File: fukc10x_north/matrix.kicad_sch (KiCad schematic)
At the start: 247 parts

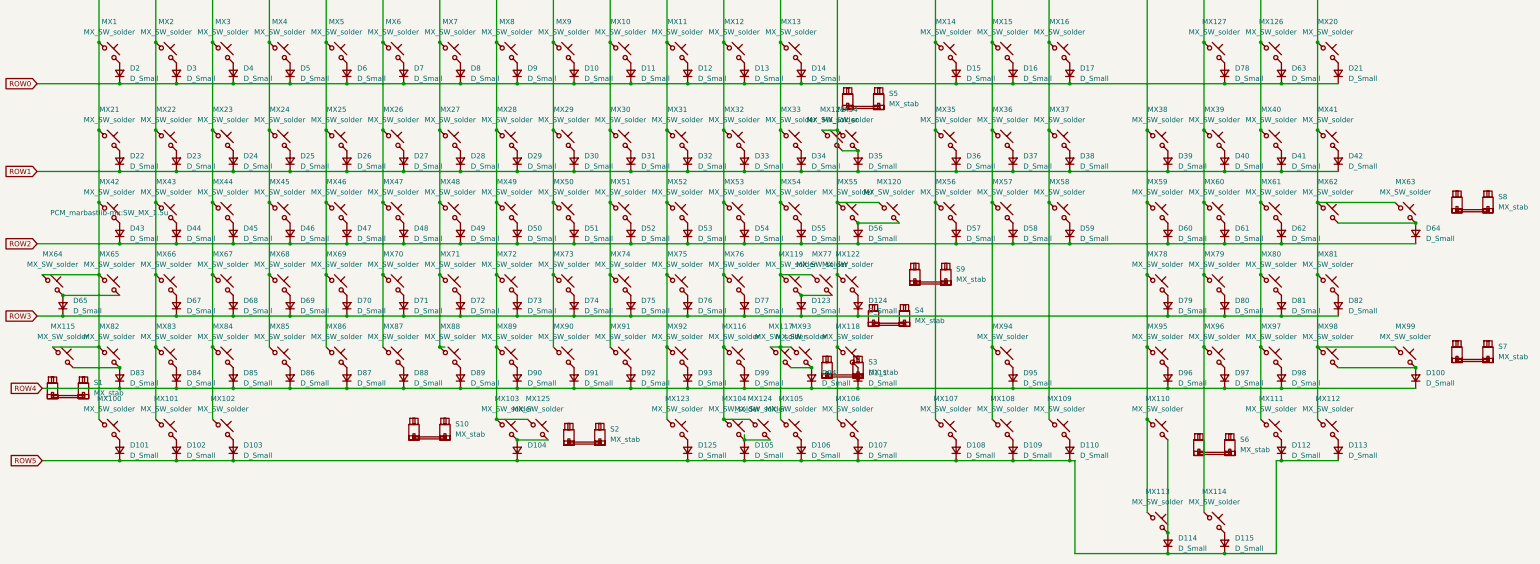
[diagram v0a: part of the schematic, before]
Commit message: updated parts for bom and stuff
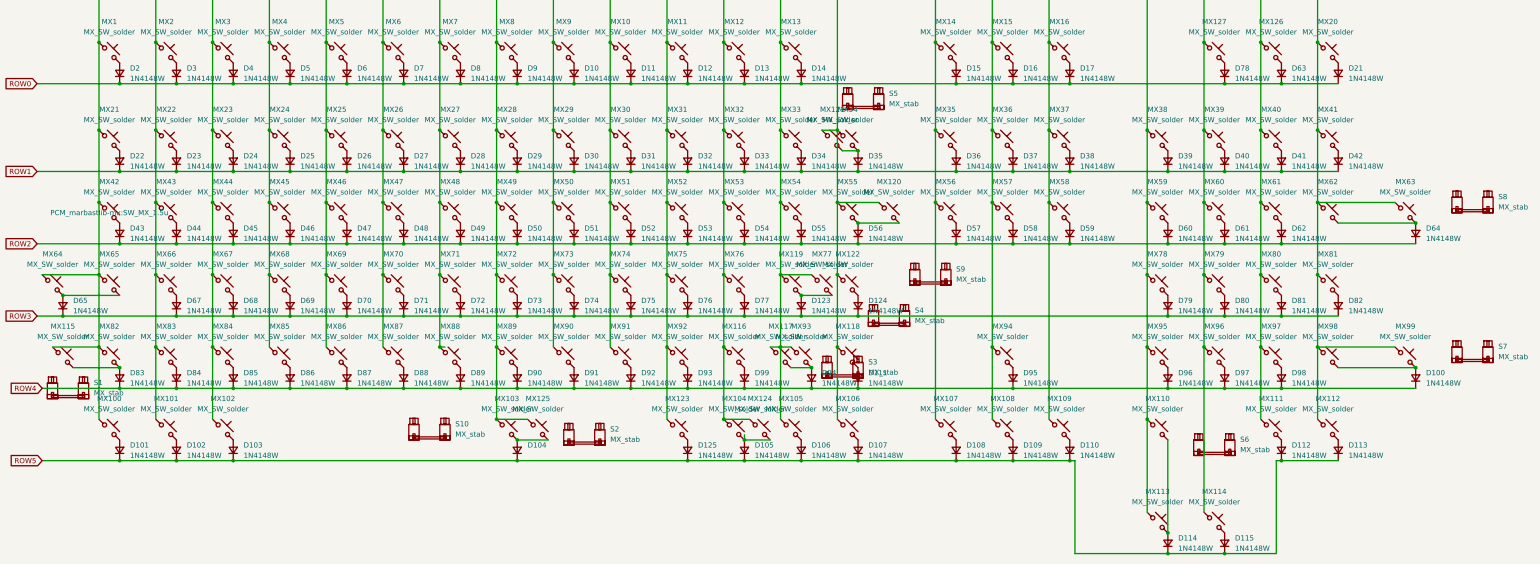
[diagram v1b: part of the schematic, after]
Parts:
- D10, D100, D101, D102, D103, D104, D105, D106, D107, D108, D109, D11, D110, D111, D112, D113, D114, D115, D12, D123, D124, D125, D13, D14, D15, D16, D17, D2, D21, D22, D23, D24, D25, D26, D27, D28, D29, D3, D30, D31, D32, D33, D34, D35, D36, D37, D38, D39, D4, D40, D41, D42, D43, D44, D45, D46, D47, D48, D49, D5, D50, D51, D52, D53, D54, D55, D56, D57, D58, D59, D6, D60, D61, D62, D63, D64, D65, D67, D68, D69, D7, D70, D71, D72, D73, D74, D75, D76, D77, D78, D79, D8, D80, D81, D82, D83, D84, D85, D86, D87, D88, D89, D9, D90, D91, D92, D93, D94, D95, D96, D97, D98, D99: value D_Small -> 1N4148W
- MX1, MX10, MX100, MX101, MX102, MX103, MX104, MX105, MX106, MX107, MX108, MX109, MX11, MX110, MX111, MX112, MX113, MX114, MX115, MX116, MX117, MX118, MX119, MX12, MX120, MX121, MX122, MX123, MX124, MX125, MX126, MX127, MX13, MX14, MX15, MX16, MX2, MX20, MX21, MX22, MX23, MX24, MX25, MX26, MX27, MX28, MX29, MX3, MX30, MX31, MX32, MX33, MX34, MX35, MX36, MX37, MX38, MX39, MX4, MX40, MX41, MX42, MX43, MX44, MX45, MX46, MX47, MX48, MX49, MX5, MX50, MX51, MX52, MX53, MX54, MX55, MX56, MX57, MX58, MX59, MX6, MX60, MX61, MX62, MX63, MX64, MX65, MX66, MX67, MX68, MX69, MX7, MX70, MX71, MX72, MX73, MX74, MX75, MX76, MX77, MX78, MX79, MX8, MX80, MX81, MX82, MX83, MX84, MX85, MX86, MX87, MX88, MX89, MX9, MX90, MX91, MX92, MX93, MX94, MX95, MX96, MX97, MX98, MX99, S1, S10, S2, S3, S4, S5, S6, S7, S8, S9: now left out of the parts list

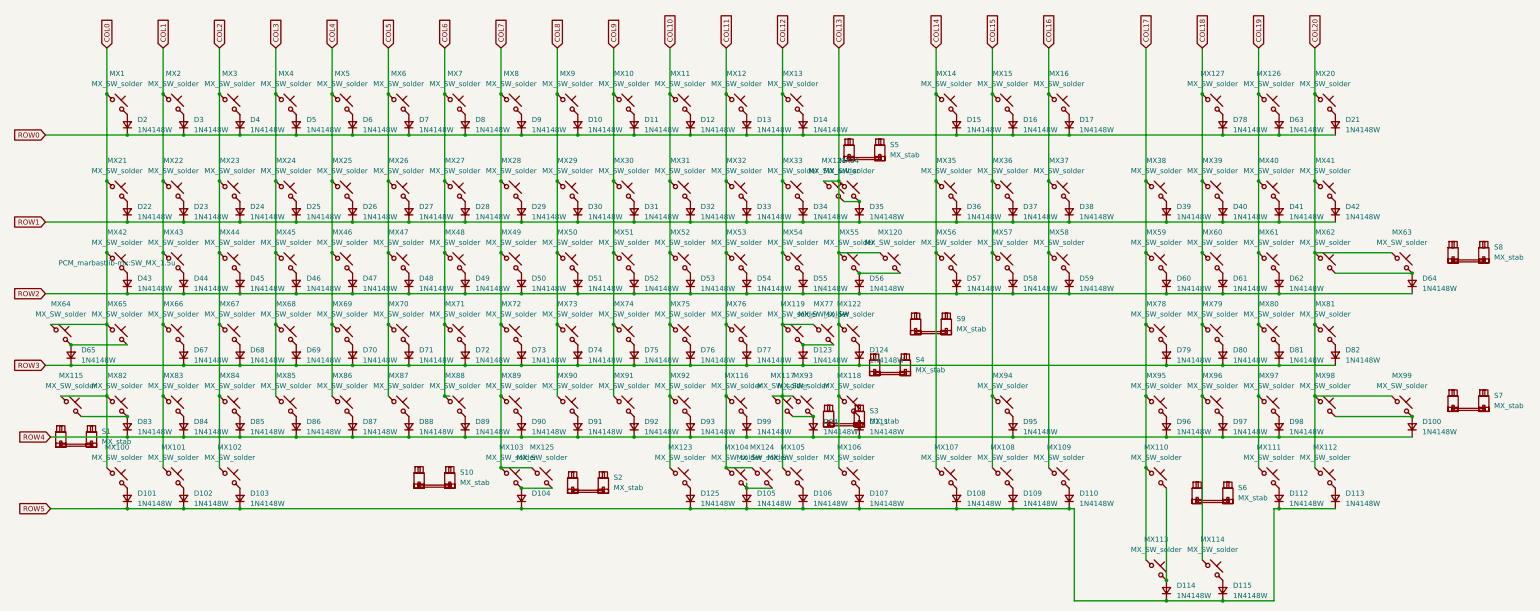
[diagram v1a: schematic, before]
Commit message: fixed some routing, changed footprints from marbastler to acheron alexandria lib (although with rotated switches(kinda cursed))
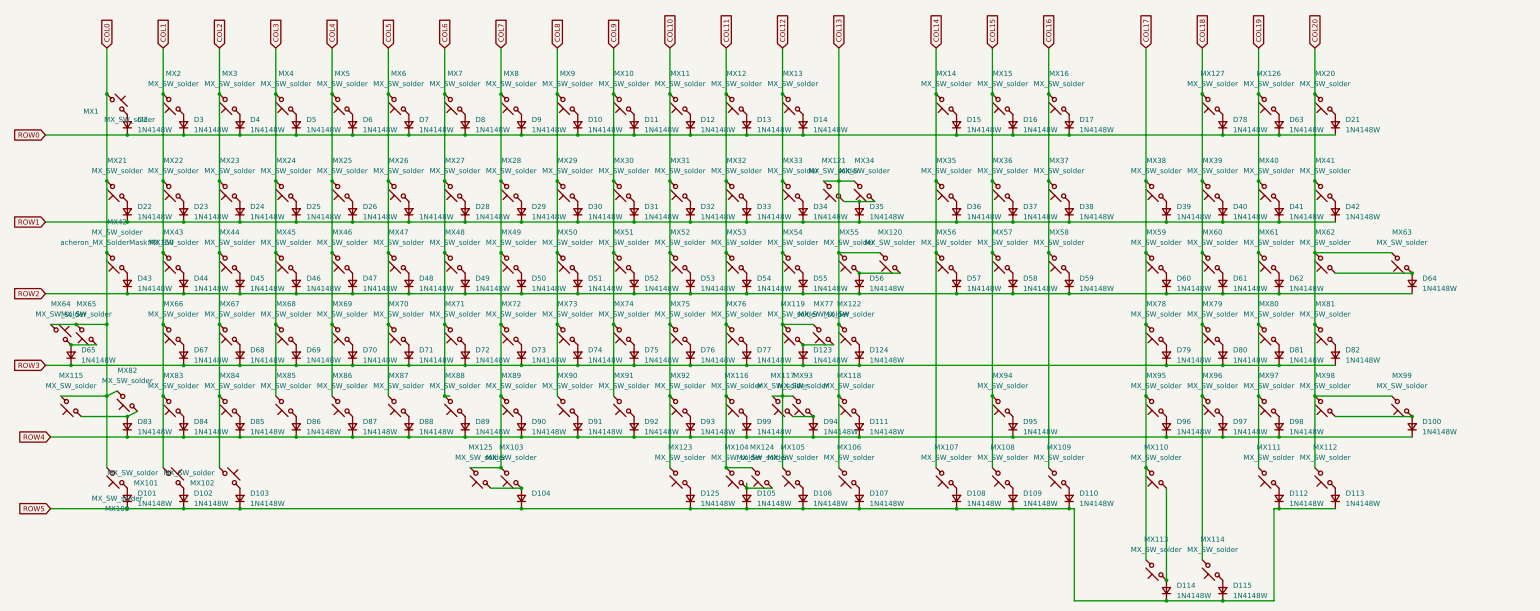
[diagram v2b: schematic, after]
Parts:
- removed S1, S4: MX_stab, PCM_marbastlib-mx:STAB_MX_2.25u, symbol PCM_marbastlib-mx:MX_stab
- removed S10: MX_stab, PCM_marbastlib-mx:STAB_MX_6u, symbol PCM_marbastlib-mx:MX_stab
- removed S2: MX_stab, PCM_marbastlib-mx:STAB_MX_7u, symbol PCM_marbastlib-mx:MX_stab
- removed S3: MX_stab, PCM_marbastlib-mx:STAB_MX_2.75u, symbol PCM_marbastlib-mx:MX_stab
- removed S5, S6, S7, S8: MX_stab, PCM_marbastlib-mx:STAB_MX_2u, symbol PCM_marbastlib-mx:MX_stab
- removed S9: MX_stab, PCM_marbastlib-mx:STAB_MX_ISO-ROT, symbol PCM_marbastlib-mx:MX_stab
- MX1, MX10, MX101, MX105, MX107, MX108, MX109, MX11, MX110, MX111, MX112, MX113, MX114, MX116, MX118, MX119, MX12, MX121, MX122, MX124, MX126, MX127, MX13, MX14, MX15, MX16, MX2, MX20, MX21, MX22, MX23, MX24, MX25, MX26, MX27, MX28, MX29, MX3, MX30, MX31, MX32, MX33, MX35, MX36, MX37, MX38, MX39, MX4, MX40, MX41, MX43, MX44, MX45, MX46, MX47, MX48, MX49, MX5, MX50, MX51, MX52, MX53, MX54, MX56, MX57, MX58, MX59, MX6, MX60, MX61, MX63, MX66, MX67, MX68, MX69, MX7, MX70, MX71, MX72, MX73, MX74, MX75, MX76, MX78, MX79, MX8, MX80, MX81, MX83, MX84, MX85, MX86, MX87, MX88, MX89, MX9, MX90, MX91, MX92, MX94, MX95, MX96, MX97, MX99: footprint PCM_marbastlib-mx:SW_MX_1u -> acheron_MX_SolderMask:MX100
- MX100, MX102, MX104, MX106, MX123, MX42, MX55: footprint PCM_marbastlib-mx:SW_MX_1.5u -> acheron_MX_SolderMask:MX150
- MX103: footprint PCM_marbastlib-mx:SW_MX_1u -> acheron_MX_SolderMask:MX700R
- MX115: footprint PCM_marbastlib-mx:SW_MX_1.25u -> acheron_MX_SolderMask:MX125
- MX117, MX64: footprint PCM_marbastlib-mx:SW_MX_1.75u -> acheron_MX_SolderMask:MX175
- MX120: footprint PCM_marbastlib-mx:SW_MX_1u -> acheron_MX_SolderMask:MX_ISOEnter
- MX125: footprint PCM_marbastlib-mx:SW_MX_1u -> acheron_MX_SolderMask:MX600CR
- MX34, MX82: footprint PCM_marbastlib-mx:SW_MX_1u -> acheron_MX_SolderMask:MX250
- MX62, MX98: footprint PCM_marbastlib-mx:SW_MX_1u -> acheron_MX_SolderMask:MX200V
- MX65: footprint PCM_marbastlib-mx:SW_MX_1.75u_STP_1.25 -> acheron_MX_SolderMask:MX125
- MX77: footprint PCM_marbastlib-mx:SW_MX_1u -> acheron_MX_SolderMask:MX250R
- MX93: footprint PCM_marbastlib-mx:SW_MX_1u -> acheron_MX_SolderMask:MX275
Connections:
- net COL0: now also MX1.2, MX100.2, MX115.2, MX21.2, MX42.2, MX65.2, MX82.2; no longer MX1.1, MX100.1, MX115.1, MX21.1, MX42.1, MX65.1, MX82.1
- net COL1: now also MX101.2, MX2.2, MX22.2, MX43.2, MX66.2, MX83.2; no longer MX101.1, MX2.1, MX22.1, MX43.1, MX66.1, MX83.1
- net COL10: now also MX11.2, MX123.2, MX31.2, MX52.2, MX75.2, MX92.2; no longer MX11.1, MX123.1, MX31.1, MX52.1, MX75.1, MX92.1
- net COL11: now also MX104.2, MX116.2, MX12.2, MX124.2, MX32.2, MX53.2, MX76.2; no longer MX104.1, MX116.1, MX12.1, MX124.1, MX32.1, MX53.1, MX76.1
- net COL12: now also MX105.2, MX117.2, MX119.2, MX13.2, MX33.2, MX54.2, MX77.2, MX93.2; no longer MX105.1, MX117.1, MX119.1, MX13.1, MX33.1, MX54.1, MX77.1, MX93.1
- net COL13: now also MX106.2, MX118.2, MX120.2, MX121.2, MX122.2, MX34.2, MX55.2; no longer MX106.1, MX118.1, MX120.1, MX121.1, MX122.1, MX34.1, MX55.1
- net COL14: now also MX107.2, MX14.2, MX35.2, MX56.2; no longer MX107.1, MX14.1, MX35.1, MX56.1
- net COL15: now also MX108.2, MX15.2, MX36.2, MX57.2, MX94.2; no longer MX108.1, MX15.1, MX36.1, MX57.1, MX94.1
- net COL16: now also MX109.2, MX16.2, MX37.2, MX58.2; no longer MX109.1, MX16.1, MX37.1, MX58.1
- net COL17: now also MX110.2, MX113.2, MX38.2, MX59.2, MX78.2, MX95.2; no longer MX110.1, MX113.1, MX38.1, MX59.1, MX78.1, MX95.1
- net COL18: now also MX114.2, MX127.2, MX39.2, MX60.2, MX79.2, MX96.2; no longer MX114.1, MX127.1, MX39.1, MX60.1, MX79.1, MX96.1
- net COL19: now also MX111.2, MX126.2, MX40.2, MX61.2, MX80.2, MX97.2; no longer MX111.1, MX126.1, MX40.1, MX61.1, MX80.1, MX97.1
- net COL2: now also MX102.2, MX23.2, MX3.2, MX44.2, MX67.2, MX84.2; no longer MX102.1, MX23.1, MX3.1, MX44.1, MX67.1, MX84.1
- net COL20: now also MX112.2, MX20.2, MX41.2, MX62.2, MX63.2, MX81.2, MX98.2, MX99.2; no longer MX112.1, MX20.1, MX41.1, MX62.1, MX63.1, MX81.1, MX98.1, MX99.1
- net COL3: now also MX24.2, MX4.2, MX45.2, MX68.2, MX85.2; no longer MX24.1, MX4.1, MX45.1, MX68.1, MX85.1
- net COL4: now also MX25.2, MX46.2, MX5.2, MX69.2, MX86.2; no longer MX25.1, MX46.1, MX5.1, MX69.1, MX86.1
- net COL5: now also MX26.2, MX47.2, MX6.2, MX70.2, MX87.2; no longer MX26.1, MX47.1, MX6.1, MX70.1, MX87.1
- net COL6: now also MX27.2, MX48.2, MX7.2, MX71.2, MX88.2; no longer MX27.1, MX48.1, MX7.1, MX71.1, MX88.1
- net COL7: now also MX103.2, MX125.2, MX28.2, MX49.2, MX72.2, MX8.2, MX89.2; no longer MX103.1, MX125.1, MX28.1, MX49.1, MX72.1, MX8.1, MX89.1
- net COL8: now also MX29.2, MX50.2, MX73.2, MX9.2, MX90.2; no longer MX29.1, MX50.1, MX73.1, MX9.1, MX90.1
- net COL9: now also MX10.2, MX30.2, MX51.2, MX74.2, MX91.2; no longer MX10.1, MX30.1, MX51.1, MX74.1, MX91.1
- net at D98.2 (A): now also MX97.1; no longer MX97.2
- net at D77.2 (A): now also MX76.1; no longer MX76.2
- net at D34.2 (A): now also MX33.1; no longer MX33.2
- net at D15.2 (A): now also MX14.1; no longer MX14.2
- net at D78.2 (A): now also MX127.1; no longer MX127.2
- net at D53.2 (A): now also MX52.1; no longer MX52.2
- net at D45.2 (A): now also MX44.1; no longer MX44.2
- net at D4.2 (A): now also MX3.1; no longer MX3.2
- net at D42.2 (A): now also MX41.1; no longer MX41.2
- net at D80.2 (A): now also MX79.1; no longer MX79.2
- net at D90.2 (A): now also MX89.1; no longer MX89.2
- net at D12.2 (A): now also MX11.1; no longer MX11.2
- net at D29.2 (A): now also MX28.1; no longer MX28.2
- net at D95.2 (A): now also MX94.1; no longer MX94.2
- net at D46.2 (A): now also MX45.1; no longer MX45.2
- net at D87.2 (A): now also MX86.1; no longer MX86.2
- net at D59.2 (A): now also MX58.1; no longer MX58.2
- net at D79.2 (A): now also MX78.1; no longer MX78.2
- net at D41.2 (A): now also MX40.1; no longer MX40.2
- net at D111.2 (A): now also MX118.1; no longer MX118.2
- net at D75.2 (A): now also MX74.1; no longer MX74.2
- net at D43.2 (A): now also MX42.1; no longer MX42.2
- net at D24.2 (A): now also MX23.1; no longer MX23.2
- net at D27.2 (A): now also MX26.1; no longer MX26.2
- net at D21.2 (A): now also MX20.1; no longer MX20.2
- net at D2.2 (A): now also MX1.1; no longer MX1.2
- net at D62.2 (A): now also MX61.1; no longer MX61.2
- net at D36.2 (A): now also MX35.1; no longer MX35.2
- net at D31.2 (A): now also MX30.1; no longer MX30.2
- net at D30.2 (A): now also MX29.1; no longer MX29.2
- net at D25.2 (A): now also MX24.1; no longer MX24.2
- net at D16.2 (A): now also MX15.1; no longer MX15.2
- net at D74.2 (A): now also MX73.1; no longer MX73.2
- net at D84.2 (A): now also MX83.1; no longer MX83.2
- net at D85.2 (A): now also MX84.1; no longer MX84.2
- net at D28.2 (A): now also MX27.1; no longer MX27.2
- net at D63.2 (A): now also MX126.1; no longer MX126.2
- net at D106.2 (A): now also MX105.1; no longer MX105.2
- net at D96.2 (A): now also MX95.1; no longer MX95.2
- net at D99.2 (A): now also MX116.1; no longer MX116.2
- net at D61.2 (A): now also MX60.1; no longer MX60.2
- net at D51.2 (A): now also MX50.1; no longer MX50.2
- net at D65.2 (A), MX64.2: now also MX65.1; no longer MX65.2
- net at D13.2 (A): now also MX12.1; no longer MX12.2
- net at D73.2 (A): now also MX72.1; no longer MX72.2
- net at D60.2 (A): now also MX59.1; no longer MX59.2
- net at D93.2 (A): now also MX92.1; no longer MX92.2
- net at D97.2 (A): now also MX96.1; no longer MX96.2
- net at D86.2 (A): now also MX85.1; no longer MX85.2
- net at D44.2 (A): now also MX43.1; no longer MX43.2
- net at D109.2 (A): now also MX108.1; no longer MX108.2
- net at D6.2 (A): now also MX5.1; no longer MX5.2
- net at D49.2 (A): now also MX48.1; no longer MX48.2
- net at D32.2 (A): now also MX31.1; no longer MX31.2
- net at D54.2 (A): now also MX53.1; no longer MX53.2
- net at D82.2 (A): now also MX81.1; no longer MX81.2
- net at D47.2 (A): now also MX46.1; no longer MX46.2
- net at D101.2 (A): now also MX100.1; no longer MX100.2
- net at D33.2 (A): now also MX32.1; no longer MX32.2
- net at D72.2 (A): now also MX71.1; no longer MX71.2
- net at D50.2 (A): now also MX49.1; no longer MX49.2
- net at D26.2 (A): now also MX25.1; no longer MX25.2
- net at D14.2 (A): now also MX13.1; no longer MX13.2
- net at D3.2 (A): now also MX2.1; no longer MX2.2
- net at D40.2 (A): now also MX39.1; no longer MX39.2
- net at D102.2 (A): now also MX101.1; no longer MX101.2
- net at D88.2 (A): now also MX87.1; no longer MX87.2
- net at D125.2 (A): now also MX123.1; no longer MX123.2
- net at D5.2 (A): now also MX4.1; no longer MX4.2
- net at D81.2 (A): now also MX80.1; no longer MX80.2
- net at D68.2 (A): now also MX67.1; no longer MX67.2
- net at D52.2 (A): now also MX51.1; no longer MX51.2
- net at D91.2 (A): now also MX90.1; no longer MX90.2
- net at D58.2 (A): now also MX57.1; no longer MX57.2
- net at D124.2 (A): now also MX122.1; no longer MX122.2
- net at D10.2 (A): now also MX9.1; no longer MX9.2
- net at D23.2 (A): now also MX22.1; no longer MX22.2
- net at D76.2 (A): now also MX75.1; no longer MX75.2
- net at D37.2 (A): now also MX36.1; no longer MX36.2
- net at D11.2 (A): now also MX10.1; no longer MX10.2
- net at D113.2 (A): now also MX112.1; no longer MX112.2
- net at D108.2 (A): now also MX107.1; no longer MX107.2
- net at D17.2 (A): now also MX16.1; no longer MX16.2
- net at D70.2 (A): now also MX69.1; no longer MX69.2
- net at D112.2 (A): now also MX111.1; no longer MX111.2
- net at D92.2 (A): now also MX91.1; no longer MX91.2
- net at D89.2 (A): now also MX88.1; no longer MX88.2
- net at D22.2 (A): now also MX21.1; no longer MX21.2
- net at D107.2 (A): now also MX106.1; no longer MX106.2
- net at D103.2 (A): now also MX102.1; no longer MX102.2
- net at D9.2 (A): now also MX8.1; no longer MX8.2
- net at D38.2 (A): now also MX37.1; no longer MX37.2
- net at D115.2 (A): now also MX114.1; no longer MX114.2
- net at D39.2 (A): now also MX38.1; no longer MX38.2
- net at D7.2 (A): now also MX6.1; no longer MX6.2
- net at D110.2 (A): now also MX109.1; no longer MX109.2
- net at D71.2 (A): now also MX70.1; no longer MX70.2
- net at D55.2 (A): now also MX54.1; no longer MX54.2
- net at D69.2 (A): now also MX68.1; no longer MX68.2
- net at D48.2 (A): now also MX47.1; no longer MX47.2
- net at D67.2 (A): now also MX66.1; no longer MX66.2
- net at D8.2 (A): now also MX7.1; no longer MX7.2
- net at D57.2 (A): now also MX56.1; no longer MX56.2
- new net: D94.2 (A), MX117.1, MX93.1
- new net: D56.2 (A), MX120.1, MX55.1
- new net: D35.2 (A), MX121.1, MX34.1
- new net: D114.2 (A), MX110.1, MX113.1
- new net: D105.2 (A), MX104.1, MX124.1
- new net: D123.2 (A), MX119.1, MX77.1
- new net: D104.2 (A), MX103.1, MX125.1
- new net: D100.2 (A), MX98.1, MX99.1
- new net: D83.2 (A), MX115.1, MX82.1
- new net: D64.2 (A), MX62.1, MX63.1
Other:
- moved on the sheet: MX1, MX10, MX100, MX101, MX102, MX103, MX104, MX105, MX106, MX107, MX108, MX109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

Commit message: fixed some shenanaigans
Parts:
- MX110: footprint acheron_MX_SolderMask:MX100 -> acheron_MX_SolderMask:MX200R
- MX77: footprint acheron_MX_SolderMask:MX250R -> acheron_MX_SolderMask:MX225R
- MX82: footprint acheron_MX_SolderMask:MX250 -> acheron_MX_SolderMask:MX225
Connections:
- net COL0: now also MX64.2; no longer MX64.1
- net at D65.2 (A), MX65.1: now also MX64.1; no longer MX64.2
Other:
- moved on the sheet: MX64
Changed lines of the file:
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@@
 	)
 	(junction
+		(at 27.94 95.25)
+		(diameter 0)
+		(color 0 0 0 0)
+	)
+	(junction
 		(at 97.79 64.77)
 		(diameter 0)
@@
 	)
 	(junction
-		(at 27.94 95.25)
-		(diameter 0)
-		(color 0 0 0 0)
-	)
-	(junction
 		(at 27.94 100.33)
 		(diameter 0)
@@
 	(symbol
 		(lib_id "PCM_marbastlib-mx:MX_SW_solder")
-		(at 25.4 92.71 0)
+		(at 25.4 92.71 180)
 		(unit 1)
 		(body_style 1)
@@
 			)
 		)
-		(property "Footprint" "acheron_MX_SolderMask:MX100"
+		(property "Footprint" "acheron_MX_SolderMask:MX200R"
 			(at 297.18 128.27 0)
 			(hide yes)
@@
 			)
 		)
-		(property "Footprint" "acheron_MX_SolderMask:MX250R"
+		(property "Footprint" "acheron_MX_SolderMask:MX225R"
 			(at 214.63 92.71 0)
 			(hide yes)
@@
 			)
 		)
-		(property "Footprint" "acheron_MX_SolderMask:MX250"
+		(property "Footprint" "acheron_MX_SolderMask:MX225"
 			(at 41.91 109.22 0)
 			(hide yes)

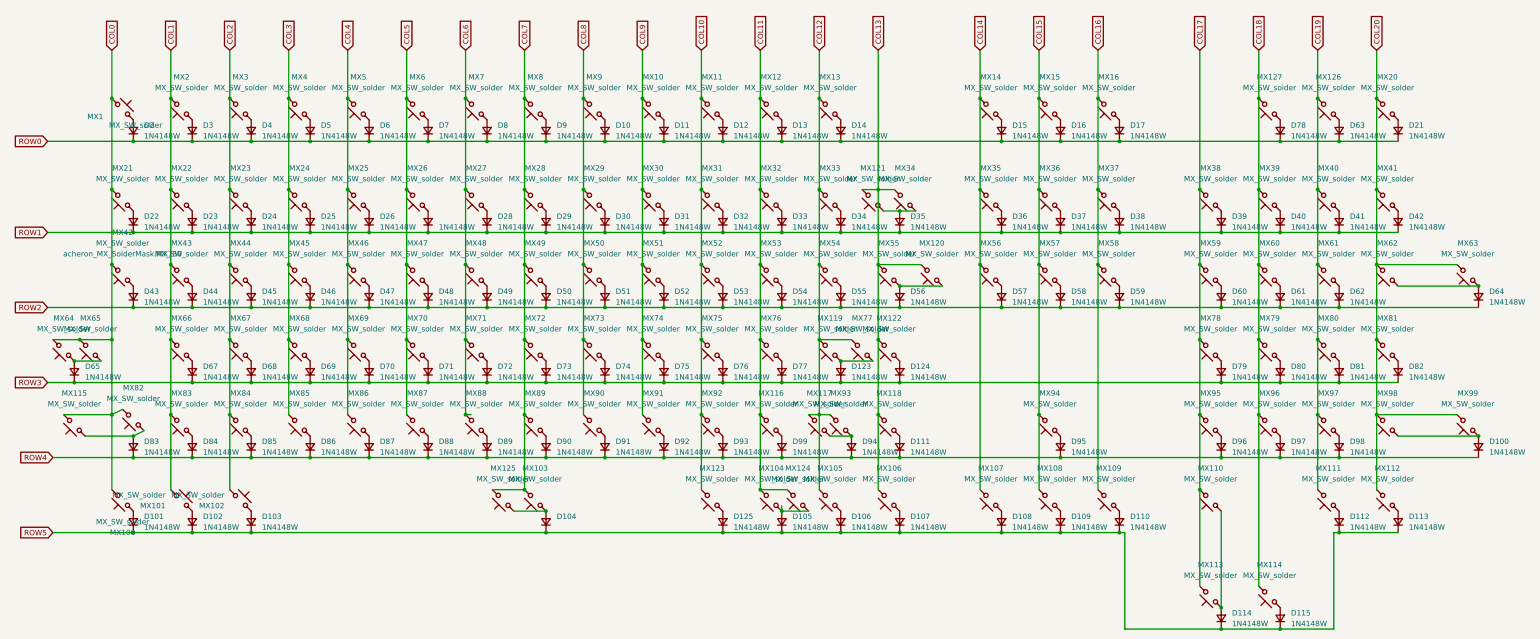
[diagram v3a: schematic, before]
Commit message: added library, fixed some routing and LED stuff
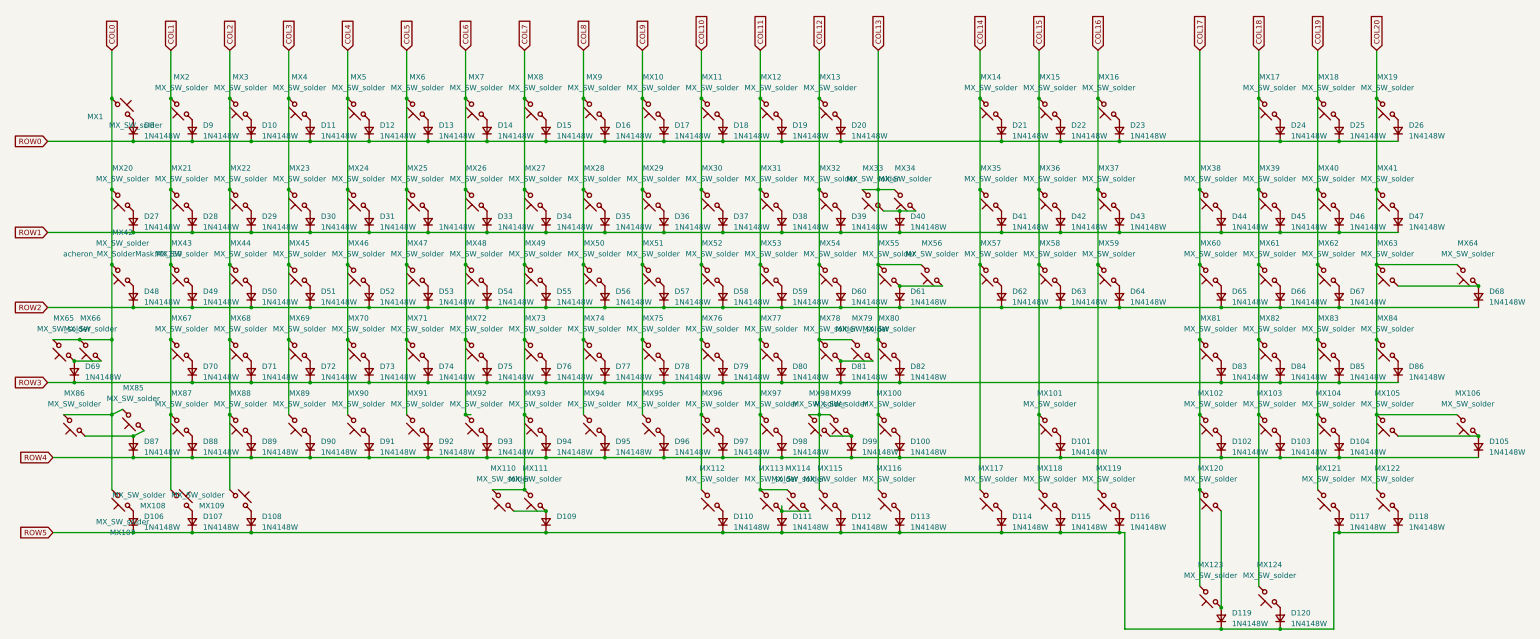
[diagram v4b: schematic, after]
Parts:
- renumbered D4 to D10, D111 to D100, D95 to D101, D96 to D102, D97 to D103, D98 to D104, D100 to D105, D101 to D106, D102 to D107, D103 to D108, D104 to D109, D5 to D11, D125 to D110, D105 to D111, D106 to D112, D107 to D113, D108 to D114, D109 to D115, D110 to D116, D112 to D117, D113 to D118, D114 to D119, D6 to D12, D115 to D120, D7 to D13, D8 to D14, D9 to D15, D10 to D16, D11 to D17, D12 to D18, D13 to D19, D14 to D20, D15 to D21, D16 to D22, D17 to D23, D78 to D24, D63 to D25, D21 to D26, D22 to D27, D23 to D28, D24 to D29, D25 to D30, D26 to D31, D27 to D32, D28 to D33, D29 to D34, D30 to D35, D31 to D36, D32 to D37, D33 to D38, D34 to D39, D35 to D40, D36 to D41, D37 to D42, D38 to D43, D39 to D44, D40 to D45, D41 to D46, D42 to D47, D43 to D48, D44 to D49, D45 to D50, D46 to D51, D47 to D52, D48 to D53, D49 to D54, D50 to D55, D51 to D56, D52 to D57, D53 to D58, D54 to D59, D55 to D60, D56 to D61, D57 to D62, D58 to D63, D59 to D64, D60 to D65, D61 to D66, D62 to D67, D64 to D68, D65 to D69, D67 to D70, D68 to D71, D69 to D72, D70 to D73, D71 to D74, D72 to D75, D73 to D76, D74 to D77, D75 to D78, D76 to D79, D2 to D8, D77 to D80, D123 to D81, D124 to D82, D79 to D83, D80 to D84, D81 to D85, D82 to D86, D83 to D87, D84 to D88, D85 to D89, D3 to D9, D86 to D90, D87 to D91, D88 to D92, D89 to D93, D90 to D94, D91 to D95, D92 to D96, D93 to D97, D99 to D98, D94 to D99, MX118 to MX100, MX94 to MX101, MX95 to MX102, MX96 to MX103, MX97 to MX104, MX98 to MX105, MX99 to MX106, MX100 to MX107, MX101 to MX108, MX102 to MX109, MX125 to MX110, MX103 to MX111, MX123 to MX112, MX104 to MX113, MX124 to MX114, MX105 to MX115, MX106 to MX116, MX107 to MX117, MX108 to MX118, MX109 to MX119, MX110 to MX120, MX111 to MX121, MX112 to MX122, MX113 to MX123, MX114 to MX124, MX127 to MX17, MX126 to MX18, MX20 to MX19, MX21 to MX20, MX22 to MX21, MX23 to MX22, MX24 to MX23, MX25 to MX24, MX26 to MX25, MX27 to MX26, MX28 to MX27, MX29 to MX28, MX30 to MX29, MX31 to MX30, MX32 to MX31, MX33 to MX32, MX121 to MX33, MX120 to MX56, MX56 to MX57, MX57 to MX58, MX58 to MX59, MX59 to MX60, MX60 to MX61, MX61 to MX62, MX62 to MX63, MX63 to MX64, MX64 to MX65, MX65 to MX66, MX66 to MX67, MX67 to MX68, MX68 to MX69, MX69 to MX70, MX70 to MX71, MX71 to MX72, MX72 to MX73, MX73 to MX74, MX74 to MX75, MX75 to MX76, MX76 to MX77, MX119 to MX78, MX77 to MX79, MX122 to MX80, MX78 to MX81, MX79 to MX82, MX80 to MX83, MX81 to MX84, MX82 to MX85, MX115 to MX86, MX83 to MX87, MX84 to MX88, MX85 to MX89, MX86 to MX90, MX87 to MX91, MX88 to MX92, MX89 to MX93, MX90 to MX94, MX91 to MX95, MX92 to MX96, MX116 to MX97, MX117 to MX98, MX93 to MX99
